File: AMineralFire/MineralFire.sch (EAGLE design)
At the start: 77 parts, among them IC1 LM358, Q1 20MHz, Q2 20MHz, Q3 2N3906, Q4 2N3906, Q5 2N3906, Q6 2N3906, Q7 2N3906, Q8 2N3906, Q9 2N3906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

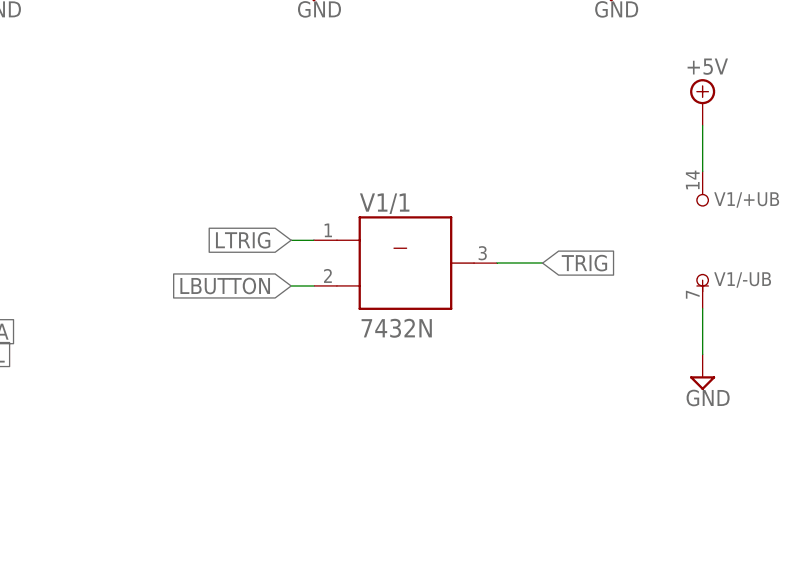
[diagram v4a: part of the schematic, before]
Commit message: updated to and gate
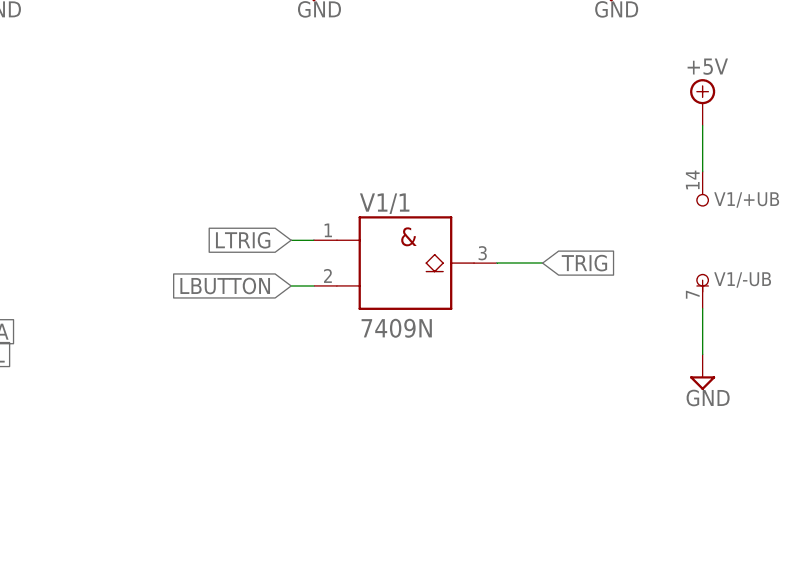
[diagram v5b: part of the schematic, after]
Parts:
- V1: value 7432N -> 7409N; device 74ttl-din:7432N -> 74ttl-din:7409N
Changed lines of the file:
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@@
 <part name="BUT" library="INSTRUO" deviceset="PB6149L-5" device="" value="PB6149L-5"/>
 <part name="BUT1" library="INSTRUO" deviceset="PB6149L-5" device="" value="PB6149L-5"/>
-<part name="V1" library="74ttl-din" deviceset="74*32" device="N"/>
-<part name="SUPPLY28" library="supply2" deviceset="+5V" device=""/>
-<part name="SUPPLY29" library="supply2" deviceset="GND" device=""/>
 <part name="C6" library="rcl" deviceset="C-EU" device="075-032X103" value="100pf"/>
 <part name="Q2" library="adafruit" deviceset="CRYSTAL" device="HC49U70" value="20MHz"/>
@@
 <part name="R30" library="SparkFun-Resistors" deviceset="330OHM" device="-HORIZ-1/10W-5%" value="330"/>
 <part name="SUPPLY41" library="supply2" library_urn="urn:adsk.eagle:library:372" deviceset="GND" device=""/>
+<part name="V1" library="74ttl-din" library_urn="urn:adsk.eagle:library:84" deviceset="74*09" device="N"/>
+<part name="SUPPLY28" library="supply2" library_urn="urn:adsk.eagle:library:372" deviceset="GND" device=""/>
+<part name="SUPPLY29" library="supply2" library_urn="urn:adsk.eagle:library:372" deviceset="+5V" device=""/>
 </parts>
 <sheets>
@@
 <instance part="BUT1" gate="G$1" x="73.66" y="132.08"/>
 <instance part="BUT1" gate="G$2" x="30.48" y="132.08"/>
-<instance part="V1" gate="/1" x="170.18" y="66.04"/>
-<instance part="V1" gate="/+UB" x="203.2" y="73.66"/>
-<instance part="SUPPLY28" gate="+5V" x="203.2" y="83.82"/>
-<instance part="V1" gate="/-UB" x="203.2" y="63.5"/>
-<instance part="SUPPLY29" gate="GND" x="203.2" y="53.34"/>
 <instance part="C6" gate="G$1" x="271.78" y="48.26" rot="R90"/>
 <instance part="Q2" gate="G$1" x="50.8" y="205.74" rot="R90"/>
@@
 <instance part="R30" gate="G$1" x="30.48" y="114.3" rot="R90"/>
 <instance part="SUPPLY41" gate="GND" x="30.48" y="99.06"/>
+<instance part="V1" gate="/1" x="170.18" y="66.04"/>
+<instance part="V1" gate="/+UB" x="203.2" y="73.66"/>
+<instance part="V1" gate="/-UB" x="203.2" y="63.5"/>
+<instance part="SUPPLY28" gate="GND" x="203.2" y="53.34"/>
+<instance part="SUPPLY29" gate="+5V" x="203.2" y="83.82"/>
 </instances>
 <busses>
@@
 </segment>
 <segment>
-<pinref part="V1" gate="/-UB" pin="-UB"/>
-<wire x1="203.2" y1="60.96" x2="203.2" y2="55.88" width="0.1524" layer="91"/>
-<pinref part="SUPPLY29" gate="GND" pin="GND"/>
-</segment>
-<segment>
 <pinref part="C3" gate="G$1" pin="2"/>
 <wire x1="38.1" y1="210.82" x2="30.48" y2="210.82" width="0.1524" layer="91"/>
@@
 <wire x1="30.48" y1="109.22" x2="30.48" y2="101.6" width="0.1524" layer="91"/>
 <pinref part="SUPPLY41" gate="GND" pin="GND"/>
+</segment>
+<segment>
+<wire x1="203.2" y1="60.96" x2="203.2" y2="55.88" width="0.1524" layer="91"/>
+<pinref part="V1" gate="/-UB" pin="-UB"/>
+<pinref part="SUPPLY28" gate="GND" pin="GND"/>
 </segment>
 </net>
@@
 </segment>
 <segment>
-<pinref part="V1" gate="/+UB" pin="+UB"/>
-<wire x1="203.2" y1="76.2" x2="203.2" y2="81.28" width="0.1524" layer="91"/>
-<pinref part="SUPPLY28" gate="+5V" pin="+5V"/>
-</segment>
-<segment>
 <pinref part="U2" gate="G$1" pin="AVCC"/>
 <wire x1="58.42" y1="228.6" x2="43.18" y2="228.6" width="0.1524" layer="91"/>
@@
 <pinref part="R27" gate="G$1" pin="2"/>
 </segment>
+<segment>
+<wire x1="203.2" y1="76.2" x2="203.2" y2="81.28" width="0.1524" layer="91"/>
+<pinref part="V1" gate="/+UB" pin="+UB"/>
+<pinref part="SUPPLY29" gate="+5V" pin="+5V"/>
+</segment>
 </net>
 <net name="MISO" class="0">
@@
 </segment>
 <segment>
-<pinref part="V1" gate="/1" pin="Y"/>
 <wire x1="180.34" y1="66.04" x2="185.42" y2="66.04" width="0.1524" layer="91"/>
 <label x="185.42" y="66.04" size="1.778" layer="95" xref="yes"/>
+<pinref part="V1" gate="/1" pin="Y"/>
 </segment>
 </net>
@@
 <net name="LTRIG" class="0">
 <segment>
-<pinref part="V1" gate="/1" pin="A"/>
 <wire x1="160.02" y1="68.58" x2="157.48" y2="68.58" width="0.1524" layer="91"/>
 <label x="157.48" y="68.58" size="1.778" layer="95" rot="R180" xref="yes"/>
+<pinref part="V1" gate="/1" pin="A"/>
 </segment>
 <segment>
@@
 <net name="LBUTTON" class="0">
 <segment>
-<pinref part="V1" gate="/1" pin="B"/>
 <wire x1="160.02" y1="63.5" x2="157.48" y2="63.5" width="0.1524" layer="91"/>
 <label x="157.48" y="63.5" size="1.778" layer="95" rot="R180" xref="yes"/>
-</segment>
-<segment>
+<pinref part="V1" gate="/1" pin="B"/>
+</segment>
+<segment>
